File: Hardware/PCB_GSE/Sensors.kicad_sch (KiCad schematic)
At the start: 19 parts, among them J6 Screw_Terminal_01x04, J7 Screw_Terminal_01x04, U1 MAX6612MXK, U4 INA125UA/2K5

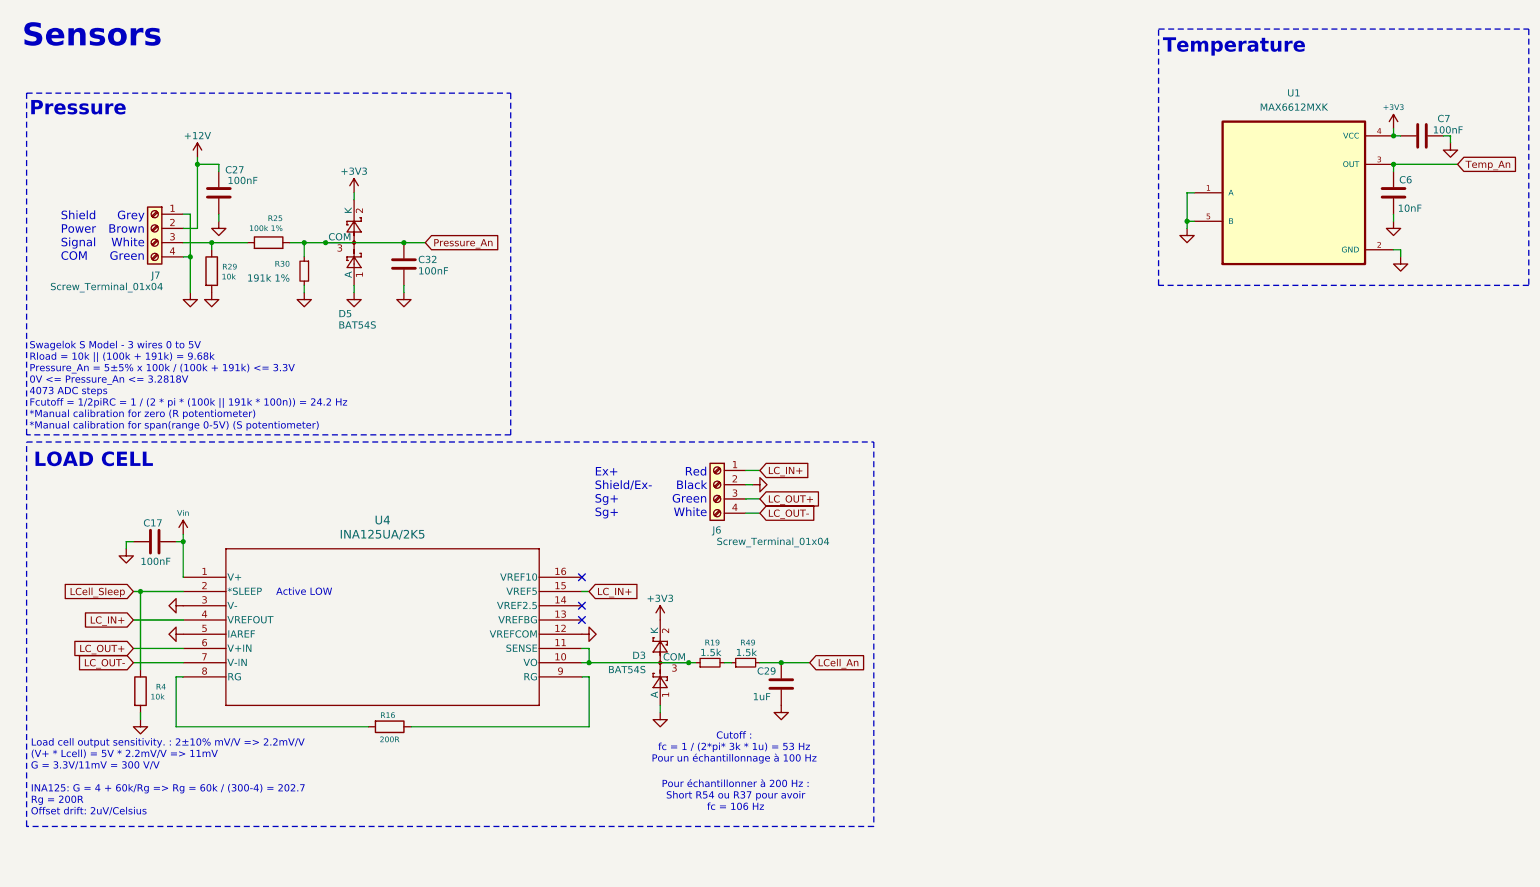
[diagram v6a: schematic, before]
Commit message: fix(gse): change Swahelok S model -> Swagelok A model (adaptable) + 100R -> 100R 1% + silkscreen
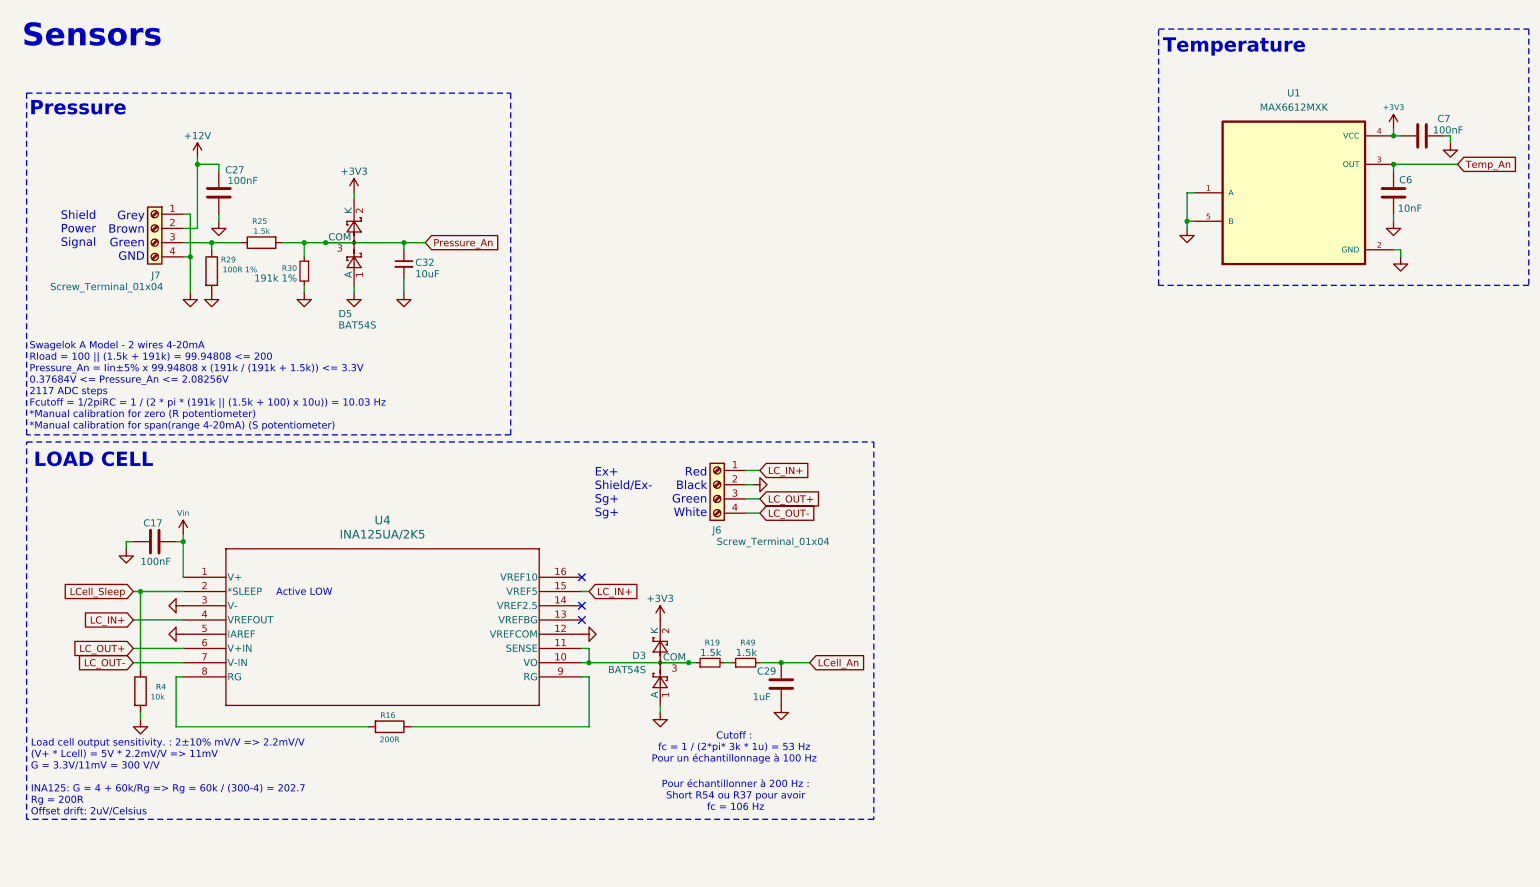
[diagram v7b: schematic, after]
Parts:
- removed C32: 100nF, Capacitor_SMD:C_0603_1608Metric, symbol Device:C
- added C32: 10uF, Capacitor_SMD:C_0805_2012Metric, symbol Device:C_Small
- R25: value 100k 1% -> 1.5k; DigiKey_Part_Number 311-100KCRCT-ND -> 311-1.50KCRCT-ND; Manufacturer_Part_Number RC0805FR-07100KL -> RC0805FR-071K5L
- R29: value 10k -> 100R 1%; DigiKey_Part_Number 541-10.0KCCT-ND -> RT0805FRE07100RL; Manufacturer_Part_Number CRCW080510K0FKEA -> YAG3360CT-ND
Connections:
- net GND: now also C32.2
- net Pressure_An: now also R25.2, C32.1; no longer R25.1
- net at J7.3 (Pin_3), R29.1: now also R25.1; no longer R25.2
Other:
- note added: "Grey Brown Green GND"
- note added: "Shield Power Signal"
- note added: "Swagelok A Model - 2 wires 4-20mA Rload = 100 || (1.5k + 191k) = 99.94808 <= 200 Pressure_An = Iin±5% x 99.94808 x (191k / (191k + 1.5k)) <= 3.3V 0.37684V <= Pressure_An <= 2.08256V 2117 ADC steps Fcutoff = 1/2piRC = 1 / (2 * pi * (191k || (1.5k + 100) x 10u)) = 10.03 Hz *Manual calibration for zero (R potentiometer) *Manual calibration for span(range 4-20mA) (S potentiometer)"
- note removed: "Grey Brown White Green"
- note removed: "Shield Power Signal COM"
- note removed: "Swagelok S Model - 3 wires 0 to 5V Rload = 10k || (100k + 191k) = 9.68k Pressure_An = 5±5% x 100k / (100k + 191k) <= 3.3V 0V <= Pressure_An <= 3.2818V 4073 ADC steps Fcutoff = 1/2piRC = 1 / (2 * pi * (100k || 191k * 100n)) = 24.2 Hz *Manual calibration for zero (R potentiometer) *Manual calibration for span(range 0-5V) (S potentiometer)"
